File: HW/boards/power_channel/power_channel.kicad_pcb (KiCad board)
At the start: 2 copper layers, 214.6 x 175.3 mm, 39 parts, among them J1 Screw_Terminal_01x02, J2 Screw_Terminal_01x02, J3 Screw_Terminal_01x03, J4 Conn_02x08_Counter_Clockwise, K1 FINDER-40.31, K2 FINDER-40.31, M1 LM2596-Buck, Q1 BC327, Q2 BC327, Q3 Q_NPN_BCE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

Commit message: routed analog section
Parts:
- moved U5 196.2 mm to (130.8, 81.3)
- moved U3 180.4 mm to (114.3, 156.2)
- moved U7 155.4 mm to (182.9, 47.0)
- moved Q4 125.2 mm to (241.3, 58.4)
- moved U1 106.8 mm to (189.2, 191.8), turned to 180 degrees
- moved R1 106.1 mm to (121.9, 193.0), turned to 180 degrees
- moved U2 101.6 mm to (119.4, 185.4)
- moved R10 90.2 mm to (149.9, 12.7), turned to 180 degrees
- moved U4 81.0 mm to (158.8, 201.9)
- moved Q1 79.0 mm to (53.3, 58.4)
- moved R18 77.8 mm to (186.7, 54.6)
- moved R8 68.0 mm to (118.1, 83.8), turned to 270 degrees
- moved R5 67.1 mm to (157.5, 207.0)
- moved J2 59.7 mm to (53.3, 142.2), turned to 90 degrees
- moved Q2 58.6 mm to (111.8, 7.62)
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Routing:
- net Net-(R6-Pad1): track 0.00 -> 24.7 mm
- net Net-(R11-Pad1): track 0.00 -> 18.2 mm
- net Net-(R12-Pad2): track 0.00 -> 17.1 mm
- net Net-(Q3-Pad1): track 0.00 -> 15.0 mm
- net Net-(Q3-Pad2): track 0.00 -> 14.6 mm
- net /analog/SET: track 0.00 -> 14.0 mm
- net Net-(R7-Pad2): track 0.00 -> 13.0 mm
- net Net-(R11-Pad2): track 0.00 -> 9.42 mm
- net GND: track 0.00 -> 6.35 mm
- net Net-(R16-Pad2): track 0.00 -> 3.81 mm
- net Net-(R14-Pad2): track 0.00 -> 3.81 mm
- net Net-(R13-Pad1): track 0.00 -> 3.81 mm
- net (no net): track 0.00 -> 0.62 mm

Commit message: reordered analog, started to internally connect digital
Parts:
- moved U4 113.4 mm to (95.2, 108.0)
- moved R5 112.5 mm to (104.1, 108.0)
- moved U1 108.5 mm to (142.2, 94.0), turned to 0 degrees
- moved U2 107.2 mm to (109.2, 78.7), turned to 270 degrees
- moved R1 107.1 mm to (102.9, 87.6), turned to 0 degrees
- moved J3 99.2 mm to (166.4, 53.3), turned to 90 degrees
- moved Q4 94.8 mm to (151.1, 87.6)
- moved K2 78.0 mm to (147.3, 76.2)
- moved D3 76.5 mm to (147.3, 82.5)
- moved D1 66.5 mm to (104.1, 80.0), turned to 90 degrees
- moved U3 65.8 mm to (102.9, 91.4), turned to 270 degrees
- moved K1 63.1 mm to (97.8, 77.5), turned to 180 degrees
- moved J4 61.2 mm to (135.9, 106.7), turned to 270 degrees
- moved R18 59.5 mm to (128.3, 43.2)
- moved R4 58.8 mm to (108.0, 91.4), turned to 270 degrees
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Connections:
- J4 pad 10: /CH6 -> /CH5
- J4 pad 11: /CH5 -> /MOSI
- J4 pad 12: /CH4 -> /CH6
- J4 pad 13: /CH3 -> /CLK
- J4 pad 14: /CH2 -> /CH7
- J4 pad 15: /CH1 -> /SCL
- J4 pad 16: /ENABLE_OUT -> /ADC_CS
- J4 pad 2: /ADC_CS -> /CH1
- J4 pad 3: /DAC_CS -> /ENABLE_OUT
- J4 pad 4: /MISO -> /CH2
- J4 pad 5: /MOSI -> /SDA
- J4 pad 6: /CLK -> /CH3
- J4 pad 7: /SCL -> /DAC_CS
- J4 pad 8: /SDA -> /CH4
- J4 pad 9: /CH7 -> /MISO
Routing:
- net /CH2: track 0.00 -> 149.1 mm
- net +15V: track 0.00 -> 65.3 mm
- net /V_OUT: track 0.00 -> 62.1 mm
- net /analog/SENSE-: track 0.00 -> 55.9 mm
- net /analog/OUT: track 0.00 -> 48.8 mm
- net /ADC_CS: track 0.00 -> 34.9 mm
- net /ENABLE_OUT: track 0.00 -> 29.2 mm
- net /CH7: track 0.00 -> 23.3 mm
- net /CH6: track 0.00 -> 21.5 mm
- net /FB: track 0.00 -> 20.3 mm
- net /CH5: track 0.00 -> 20.1 mm
- net /CH4: track 0.00 -> 19.2 mm
- net /CH3: track 0.00 -> 18.1 mm
- net Net-(D3-Pad2): track 0.00 -> 17.0 mm
- net /CH1: track 0.00 -> 16.3 mm
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- added copper zone on B.Cu, net GND
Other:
- board outline removed

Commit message: found proper relays, deleted all traces to enable heatsink
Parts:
- K1: value FINDER-40.31 -> G5Q-1A; footprint Relay_THT:Relay_SPDT_Finder_40.31 -> Relay_THT:Relay_SPST_Omron-G5Q-1A
- K2: value FINDER-40.31 -> Fujitsu_FTR-F1A; footprint Relay_THT:Relay_SPDT_Finder_40.31 -> Relay_THT:Relay_DPST_Fujitsu_FTR-F1A
- moved U2 52.8 mm to (85.1, 125.7)
- moved R1 48.3 mm to (74.9, 127.0)
- moved R14 29.3 mm to (138.4, 120.7)
- moved R2 29.3 mm to (114.3, 120.7)
- moved R4 29.3 mm to (110.5, 120.7)
- moved U3 29.3 mm to (105.4, 120.7)
- moved R5 29.3 mm to (106.7, 137.2)
- moved U4 29.3 mm to (97.8, 137.2)
- moved U1 29.3 mm to (144.8, 123.2)
- moved J4 29.3 mm to (138.4, 135.9)
- moved J2 25.7 mm to (54.6, 111.8)
- moved K2 24.1 mm to (154.9, 53.3), turned to 0 degrees
- moved K1 20.4 mm to (77.5, 76.2), turned to 0 degrees
- moved U5 1.27 mm to (132.1, 90.2)
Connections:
- J3 pad 1: /OUT -> /OUT+
- J3 pad 3: GND -> /OUT-
- M1 pad 1: Net-(K1-Pad14) -> Net-(K1-Pad3)
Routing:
- net /CH2: track 149.1 -> 0.00 mm
- net +15V: track 65.3 -> 0.00 mm
- net /V_OUT: track 62.1 -> 0.00 mm
- net /analog/SENSE-: track 55.9 -> 0.00 mm
- net /analog/OUT: track 48.8 -> 0.00 mm
- net /ADC_CS: track 34.9 -> 0.00 mm
- net /ENABLE_OUT: track 29.2 -> 0.00 mm
- net Net-(R6-Pad1): track 28.3 -> 0.00 mm
- net Net-(R11-Pad1): track 24.3 -> 0.00 mm
- net Net-(R12-Pad2): track 23.9 -> 0.00 mm
- net Net-(R7-Pad2): track 23.7 -> 0.00 mm
- net /CH7: track 23.3 -> 0.00 mm
- net /analog/SET: track 22.3 -> 0.00 mm
- net /CH6: track 21.5 -> 0.00 mm
- net /FB: track 20.3 -> 0.00 mm
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- removed copper zone on B.Cu, net GND

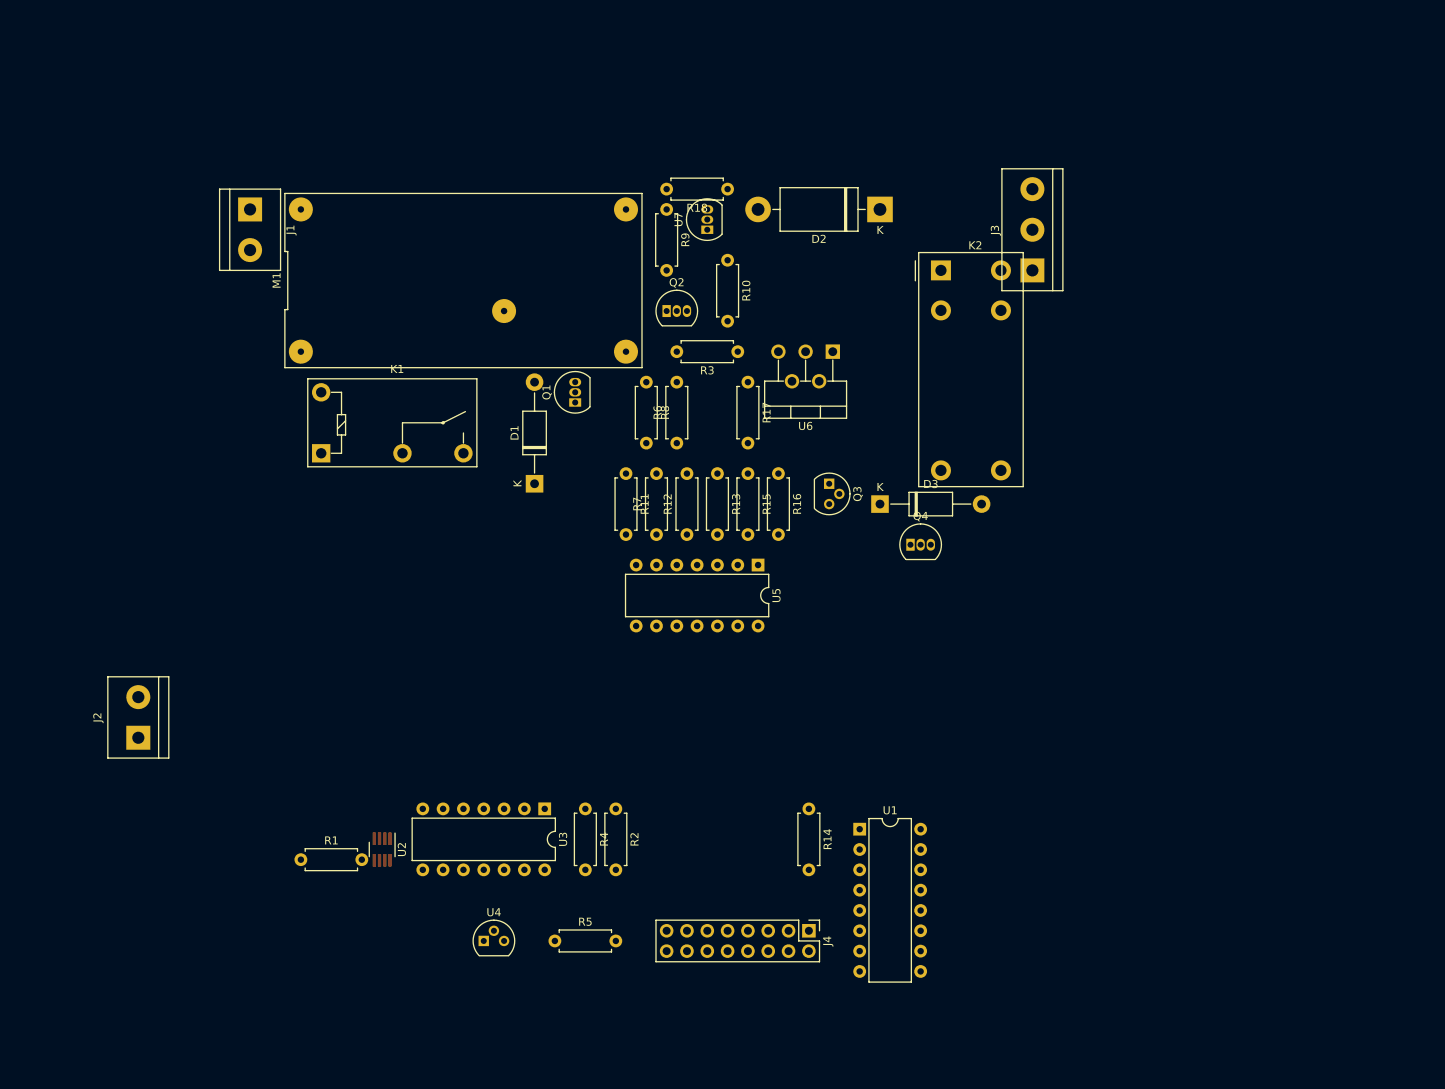
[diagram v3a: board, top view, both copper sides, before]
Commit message: further refinement of schematic, rework opamp section then done
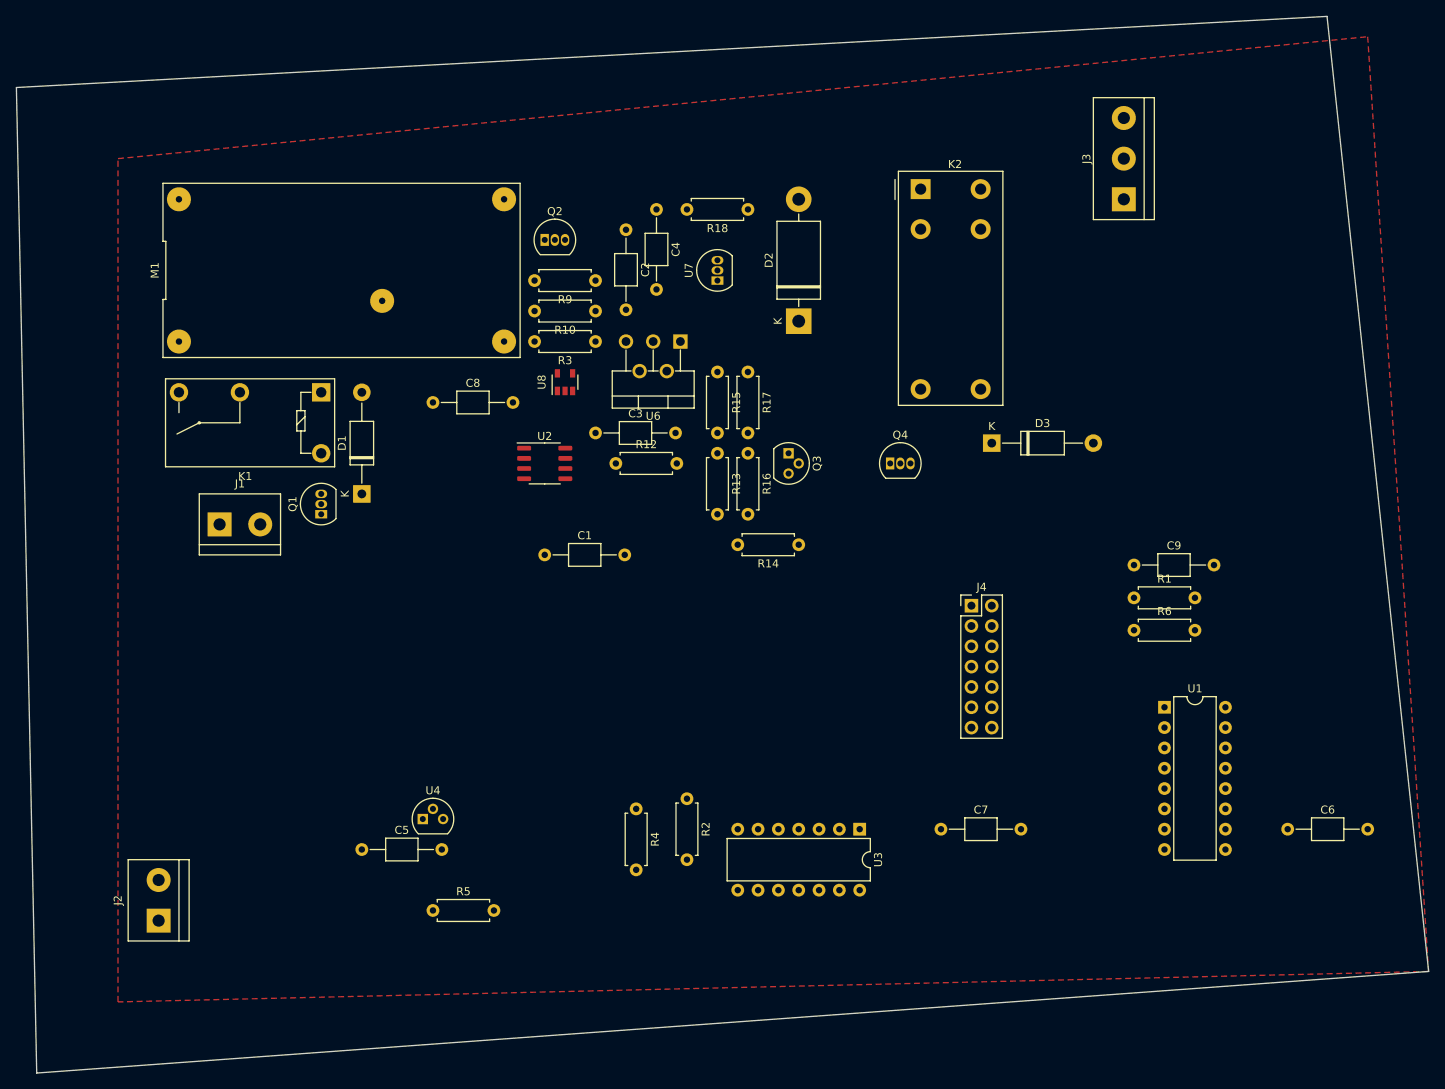
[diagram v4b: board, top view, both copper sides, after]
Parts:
- removed R11, R8: 8k2R, Resistor_THT:R_Axial_DIN0207_L6.3mm_D2.5mm_P7.62mm_Horizontal
- removed R7: 1kR, Resistor_THT:R_Axial_DIN0207_L6.3mm_D2.5mm_P7.62mm_Horizontal
- removed U5: LM324, Package_DIP:DIP-14_W7.62mm
- added C1: C, Capacitor_THT:C_Axial_L3.8mm_D2.6mm_P10.00mm_Horizontal, F.Cu at (105.4, 88.9)
- added C2: C, Capacitor_THT:C_Axial_L3.8mm_D2.6mm_P10.00mm_Horizontal, F.Cu at (115.6, 48.3)
- added C3: C, Capacitor_THT:C_Axial_L3.8mm_D2.6mm_P10.00mm_Horizontal, F.Cu at (111.8, 73.7)
- added C4: C, Capacitor_THT:C_Axial_L3.8mm_D2.6mm_P10.00mm_Horizontal, F.Cu at (119.4, 45.7)
- added C5: C, Capacitor_THT:C_Axial_L3.8mm_D2.6mm_P10.00mm_Horizontal, F.Cu at (82.5, 125.7)
- added C6: C, Capacitor_THT:C_Axial_L3.8mm_D2.6mm_P10.00mm_Horizontal, F.Cu at (198.3, 123.2)
- added C7: C, Capacitor_THT:C_Axial_L3.8mm_D2.6mm_P10.00mm_Horizontal, F.Cu at (154.9, 123.2)
- added C8: C, Capacitor_THT:C_Axial_L3.8mm_D2.6mm_P10.00mm_Horizontal, F.Cu at (91.4, 69.8)
- added C9: C, Capacitor_THT:C_Axial_L3.8mm_D2.6mm_P10.00mm_Horizontal, F.Cu at (179.1, 90.2)
- added U8: INA196, Package_TO_SOT_SMD:SOT-23-5, F.Cu at (108.0, 67.3)
- J4: value Conn_02x08_Counter_Clockwise -> Conn_02x07_Counter_Clockwise; footprint Connector_PinHeader_2.54mm:PinHeader_2x08_P2.54mm_Vertical -> Connector_PinHeader_2.54mm:PinHeader_2x07_P2.54mm_Vertical
- R6: value 1kR -> R
- U2: value INA219AIDCNR -> LM358; footprint Package_TO_SOT_SMD:SOT-23-8_Handsoldering -> Package_SO:SO-8_3.9x4.9mm_P1.27mm
- moved R1 109.2 mm to (179.1, 94.3)
- moved R6 61.8 mm to (179.1, 98.3), turned to 0 degrees
- moved U2 52.4 mm to (105.4, 77.5), turned to 0 degrees
- moved J4 45.4 mm to (158.8, 95.2), turned to 0 degrees
- moved U1 41.0 mm to (182.9, 108.0)
- moved J1 39.6 mm to (64.8, 85.1), turned to 0 degrees
- moved U3 39.5 mm to (144.8, 123.2)
- moved Q1 34.7 mm to (77.5, 83.8)
- moved R14 33.0 mm to (137.2, 87.6), turned to 180 degrees
- moved J2 23.0 mm to (57.1, 134.6)
- moved D1 21.6 mm to (82.5, 81.3)
- moved U6 19.1 mm to (122.4, 62.2)
- moved R3 17.8 mm to (111.8, 62.2)
- moved R10 17.7 mm to (111.8, 58.4), turned to 180 degrees
- moved Q2 17.6 mm to (105.4, 49.5)
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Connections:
- J3 pad 2: /V_OUT -> Net-(J3-Pad2)
- J4 pad 10: /CH5 -> /CH6
- J4 pad 11: /MOSI -> /CH5
- J4 pad 12: /CH6 -> /CH4
- J4 pad 13: /CLK -> /CH3
- J4 pad 14: /CH7 -> /CH2
- J4 pad 2: /CH1 -> /ENABLE_OUT
- J4 pad 3: /ENABLE_OUT -> /ADC_CS
- J4 pad 4: /CH2 -> /DAC_CS
- J4 pad 5: /SDA -> /MISO
- J4 pad 6: /CH3 -> /MOSI
- J4 pad 7: /DAC_CS -> /CLK
- J4 pad 8: /CH4 -> Net-(J4-Pad8)
- J4 pad 9: /MISO -> /CH7
- R1 pad 1: Net-(R1-Pad1) -> /V_Out
- R1 pad 2: GNDD -> GND
- R6 pad 1: Net-(R6-Pad1) -> /V_Out
- R6 pad 2: /analog/SENSE+ -> Net-(J3-Pad2)
- U1 pad 1: /V_OUT -> /V_Out
- U1 pad 2: /CH1 -> /I_Out
- U2 pad 1: /analog/SENSE+ -> Net-(R14-Pad2)
- U2 pad 2: /analog/SENSE- -> /analog/I_Set
- U2 pad 3: GNDD -> /I_Out
- U2 pad 4: +5V -> GND
- U2 pad 5: /SCL -> Net-(R12-Pad2)
- U2 pad 6: /SDA -> /analog/V_Set
- U2 pad 7: Net-(R1-Pad1) -> Net-(R16-Pad2)
- U2 pad 8: Net-(R1-Pad1) -> +15V
- U4 pad 1: GNDD -> GND
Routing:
- added copper zone on F.Cu, net GND
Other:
- board outline added: 176.5 x 132.1 mm

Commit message: schematic complete, placed power and analog components, preliminary placement of digital stuff, now route power
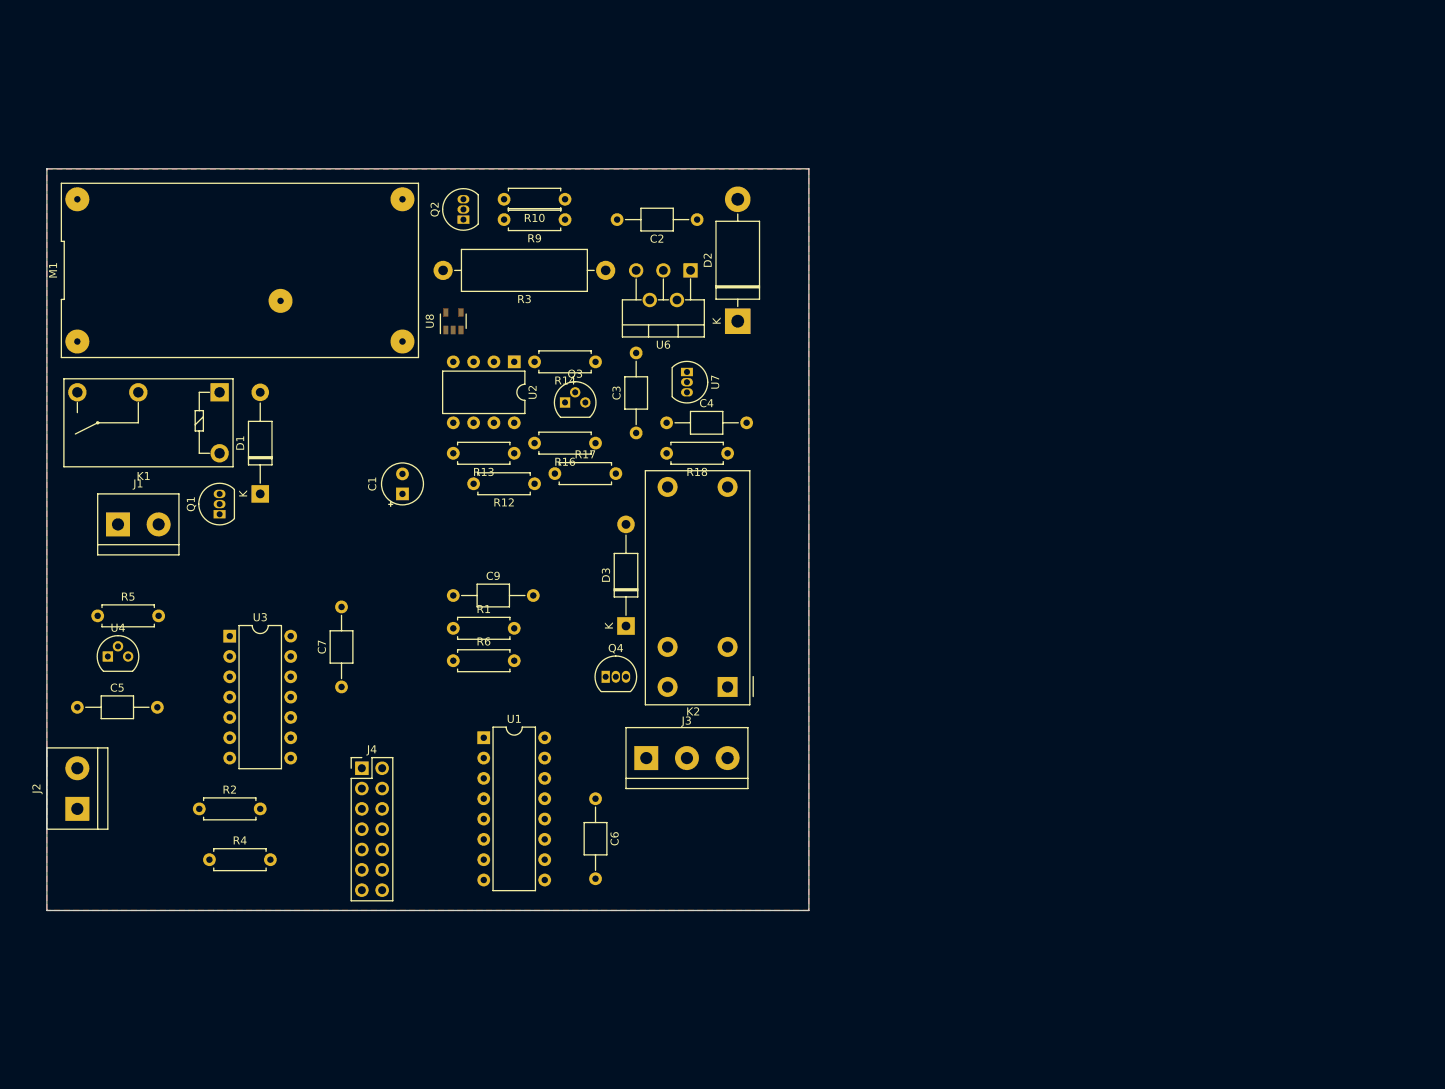
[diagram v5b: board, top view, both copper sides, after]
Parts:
- removed C8: C, Capacitor_THT:C_Axial_L3.8mm_D2.6mm_P10.00mm_Horizontal
- removed R15: 530R, Resistor_THT:R_Axial_DIN0207_L6.3mm_D2.5mm_P7.62mm_Horizontal
- C1: footprint Capacitor_THT:C_Axial_L3.8mm_D2.6mm_P10.00mm_Horizontal -> Capacitor_THT:CP_Radial_Tantal_D5.0mm_P2.50mm
- R3: footprint Resistor_THT:R_Axial_DIN0207_L6.3mm_D2.5mm_P7.62mm_Horizontal -> Resistor_THT:R_Axial_DIN0516_L15.5mm_D5.0mm_P20.32mm_Horizontal
- U2: footprint Package_SO:SO-8_3.9x4.9mm_P1.27mm -> Package_DIP:DIP-8_W7.62mm
- moved J3 91.9 mm to (118.1, 114.3), turned to 0 degrees
- moved C6 86.6 mm to (111.8, 119.4), turned to 270 degrees
- moved C9 85.2 mm to (94.0, 94.0)
- moved R1 85.2 mm to (94.0, 98.1)
- moved R6 85.2 mm to (94.0, 102.1)
- moved U1 85.2 mm to (97.8, 111.8)
- moved U3 82.4 mm to (66.0, 99.1), turned to 0 degrees
- moved J4 78.9 mm to (82.5, 115.6)
- moved C7 77.0 mm to (80.0, 105.4), turned to 90 degrees
- moved K2 66.7 mm to (128.3, 105.4), turned to 180 degrees
- moved R2 61.0 mm to (62.2, 120.7), turned to 0 degrees
- moved R5 55.8 mm to (49.5, 96.5)
- moved R4 53.7 mm to (63.5, 127.0), turned to 0 degrees
- moved D3 51.1 mm to (115.6, 97.8), turned to 90 degrees
- moved Q4 44.5 mm to (113.0, 104.1)
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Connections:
- R13 pad 1: Net-(R13-Pad1) -> /analog/SET
- U2 pad 2: /analog/I_Set -> /I_Out
- U2 pad 3: /I_Out -> /analog/I_Set
- U2 pad 5: Net-(R12-Pad2) -> /analog/V_Set
- U2 pad 6: /analog/V_Set -> Net-(R12-Pad2)
- U8 pad 4: /analog/SENSE- -> /analog/SENSE+
- U8 pad 5: /analog/SENSE+ -> /analog/SENSE-
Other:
- board size 176.5 x 132.1 mm -> 95.2 x 92.7 mm
